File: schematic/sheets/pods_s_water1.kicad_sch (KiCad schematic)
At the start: 3 parts

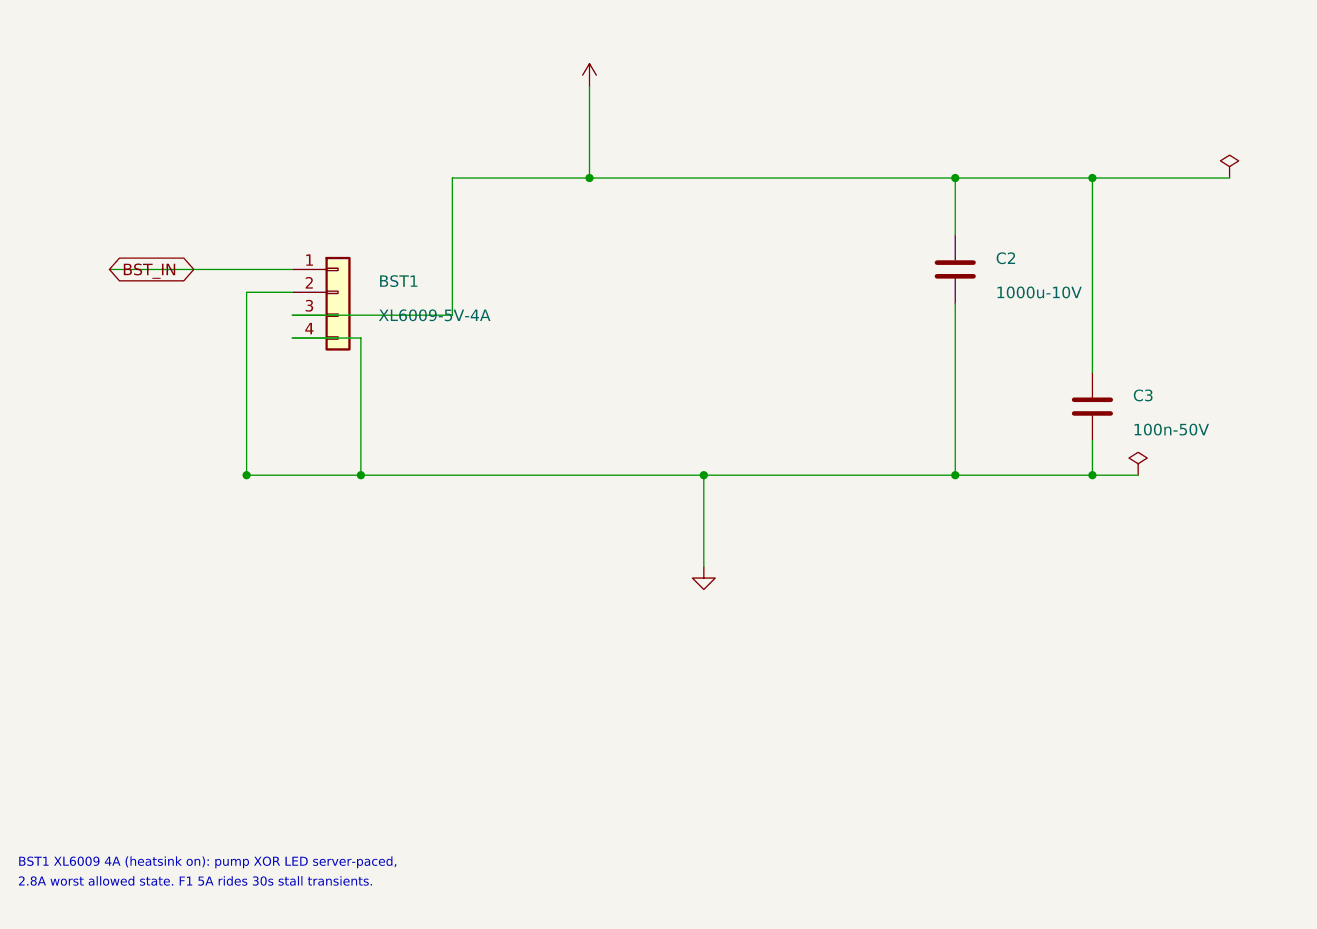
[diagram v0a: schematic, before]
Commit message: Organize schematic/: sheets/ mfg/ final/, drop sklib
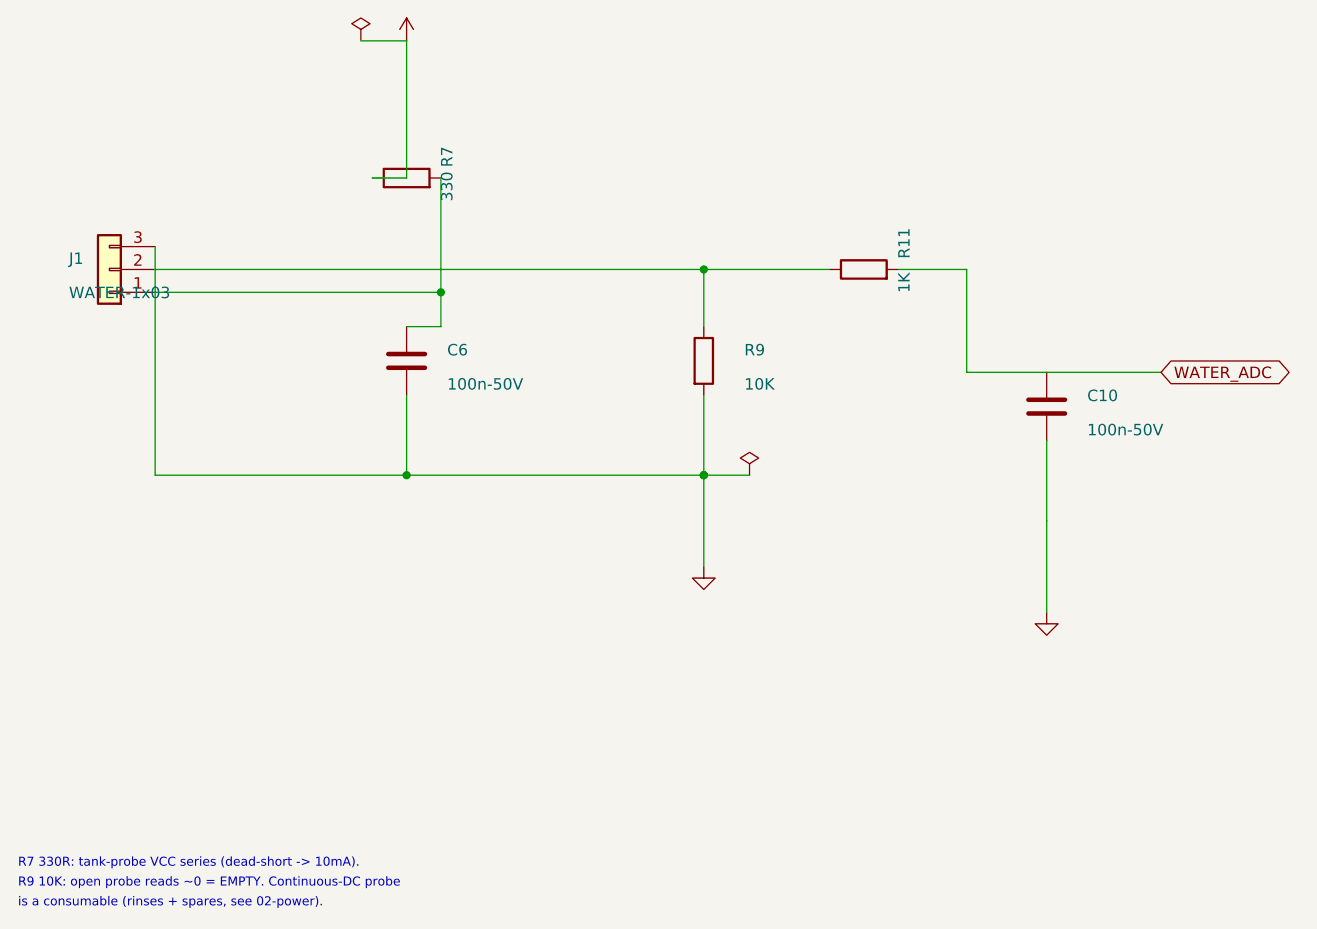
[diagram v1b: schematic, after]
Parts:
- removed BST1: XL6009-5V-4A, Connector_PinHeader_2.54mm:PinHeader_1x04_P2.54mm_Vertical, symbol Connector_Generic:Conn_01x04
- removed C2: 1000u-10V, Capacitor_THT:CP_Radial_D8.0mm_P3.50mm, symbol Device:C
- removed C3: 100n-50V, Capacitor_SMD:C_0603_1608Metric, symbol Device:C
- added C10, C6: 100n-50V, Capacitor_SMD:C_0603_1608Metric, symbol Device:C
- added J1: WATER-1x03, Connector_PinHeader_2.54mm:PinHeader_1x03_P2.54mm_Vertical, symbol Connector_Generic:Conn_01x03
- added R11: 1K, Resistor_SMD:R_0603_1608Metric, symbol Device:R
- added R7: 330, Resistor_SMD:R_0603_1608Metric, symbol Device:R
- added R9: 10K, Resistor_SMD:R_0603_1608Metric, symbol Device:R
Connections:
- net GND: now also C10.2, C6.2, J1.3 (Pin_3), R9.2
- new net: J1.2 (Pin_2), R11.1, R9.1
- new net: C6.1, J1.1 (Pin_1), R7.2
- new net +3V3: R7.1
- new net WATER_ADC: C10.1, R11.2
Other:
- note added: "R7 330R: tank-probe VCC series (dead-short -> 10mA)."
- note added: "R9 10K: open probe reads ~0 = EMPTY. Continuous-DC probe"
- note added: "is a consumable (rinses + spares, see 02-power)."
- note removed: "2.8A worst allowed state. F1 5A rides 30s stall transients."
- note removed: "BST1 XL6009 4A (heatsink on): pump XOR LED server-paced,"
